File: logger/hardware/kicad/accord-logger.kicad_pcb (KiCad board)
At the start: 2 copper layers, 120 x 80 mm, 87 parts, among them J1 Board connector 14-way, J3 Spare GP13 / switched power, J4 Reset RUN-GND, J5 SD breakout 6-way, Q5 IPD50P04P4L-11, Q6 2N3904, Q7 2N3904, U1 RaspberryPi_Pico_W, U15 MAX3485, U16 DS3231SN, U2 PC817, U3 ASSR-601JV, U6 LM2678T-5.0

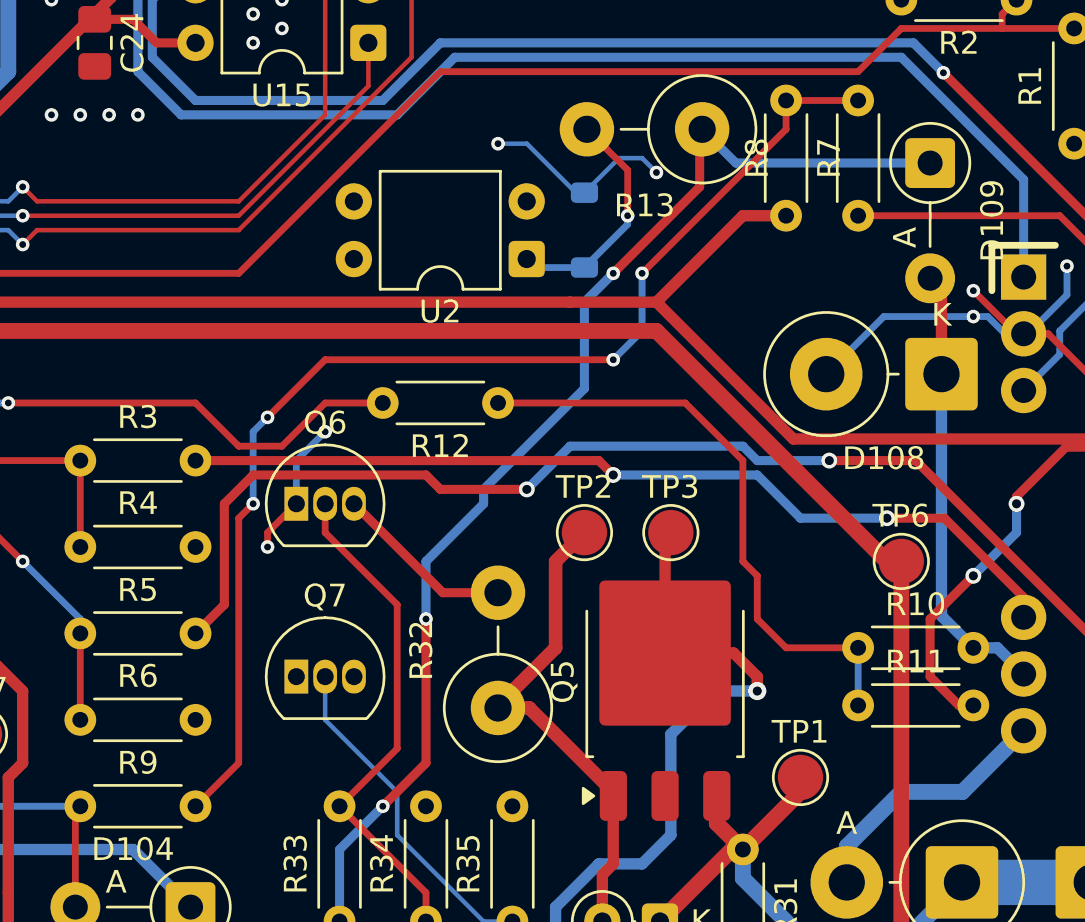
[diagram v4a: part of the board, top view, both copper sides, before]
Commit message: layout: a5_clamp and a5_reg placed and routed
Owner switched on a5_clamp (R22, D111, TP8) and a5_reg (U4, C4, C5, C6,
TP9); eight on_board flags. R22 and D111 sit right of Q5 on P12, TP8 on
the back beside them. U4 TPS70950 on the back by U2, EN open as designed;
C4 at its input (3.1 mm), C5/C6 on A5 between U4 and U2 pin 4. P_AON
runs 0.4 mm from the clamp to U4.

After review: C4 moved from the clamp to U4's input, C5/C6 spaced to
clear their courtyards, FUEL_DIV cleared of the A5 via.

Refilled scratch DRC: parity 0, no errors beyond the Pico footprint's own
paste items, unconnected only Q5's middle lead. ERC 0; full-netlist
capture 782/782; closure 67/67.

Claude-Session-ID: d2c32eb9-406b-48d8-b5b5-bb1d8d4746af
Co-Authored-By: Claude Opus 5.5 <noreply@anthropic.com>
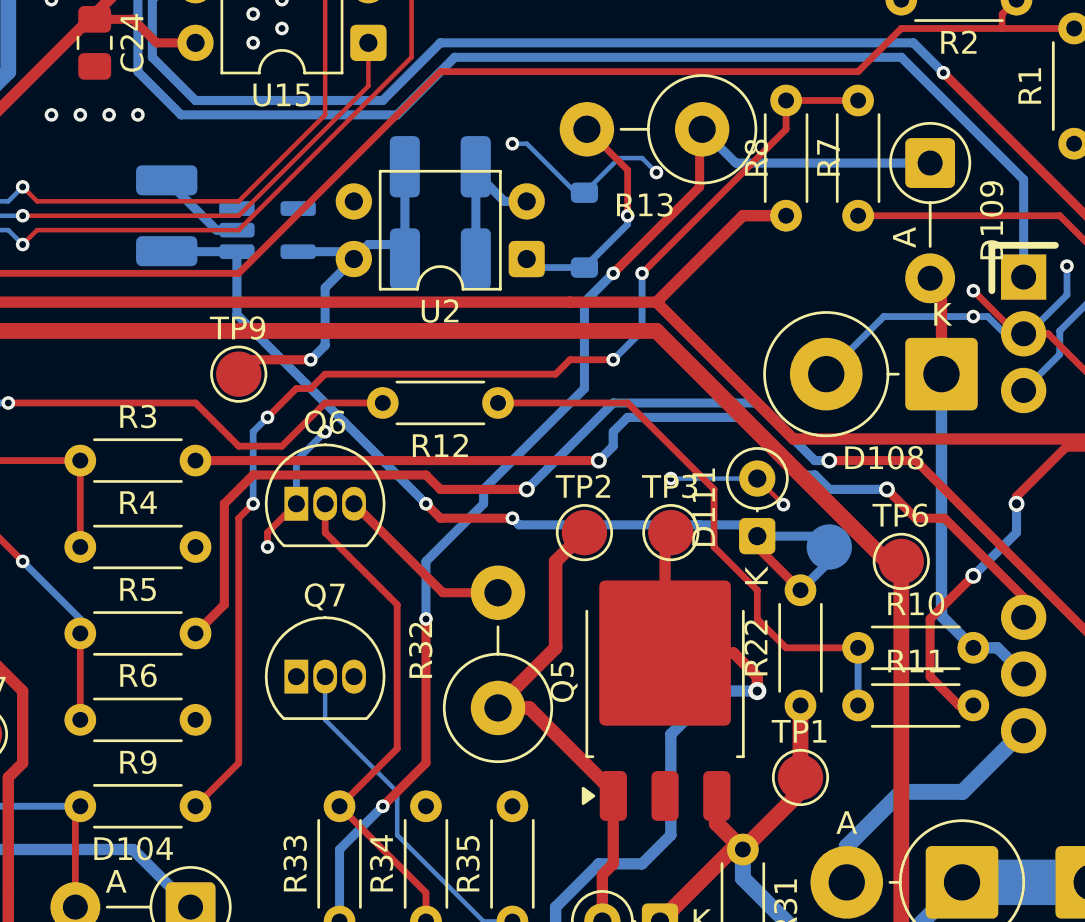
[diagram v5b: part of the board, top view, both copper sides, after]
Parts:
- added C4: 4.7uF/50V, Capacitor_SMD:C_1210_3225Metric_Pad1.33x2.70mm_HandSolder, B.Cu at (148.0, 87.0)
- added C5: 4.7uF/50V, Capacitor_SMD:C_1210_3225Metric_Pad1.33x2.70mm_HandSolder, B.Cu at (160.0, 84.8)
- added C6: 4.7uF/50V, Capacitor_SMD:C_1210_3225Metric_Pad1.33x2.70mm_HandSolder, B.Cu at (160.0, 88.9)
- added D111: BZX55C22, Diode_THT:D_DO-35_SOD27_P2.54mm_Vertical_KathodeUp, F.Cu at (174.0, 101.1)
- added R22: 820R, Resistor_THT:R_Axial_DIN0204_L3.6mm_D1.6mm_P5.08mm_Horizontal, F.Cu at (175.9, 108.6)
- added TP8: TestPoint, TestPoint:TestPoint_Pad_D2.0mm, B.Cu at (177.2, 101.6)
- added TP9: TestPoint, TestPoint:TestPoint_Pad_D2.0mm, F.Cu at (151.1, 94.0)
- added U4: TPS70950QDBVRQ1, Package_TO_SOT_SMD:SOT-23-5_HandSoldering, B.Cu at (152.4, 87.6)
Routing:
- net /P_AON: track 0.00 -> 41.8 mm, vias 0 -> 2
- net /A5: track 0.00 -> 16.9 mm, vias 0 -> 1
- net /PGND: track 79.9 -> 94.6 mm, vias 27 -> 29
- net /P12: track 34.5 -> 37.7 mm
- net /B1_TAP: track 39.9 -> 41.8 mm
- net /C14_TAP: track 53.2 -> 54.8 mm
- net /SUPPLY_DIV: track 26.6 -> 25.1 mm

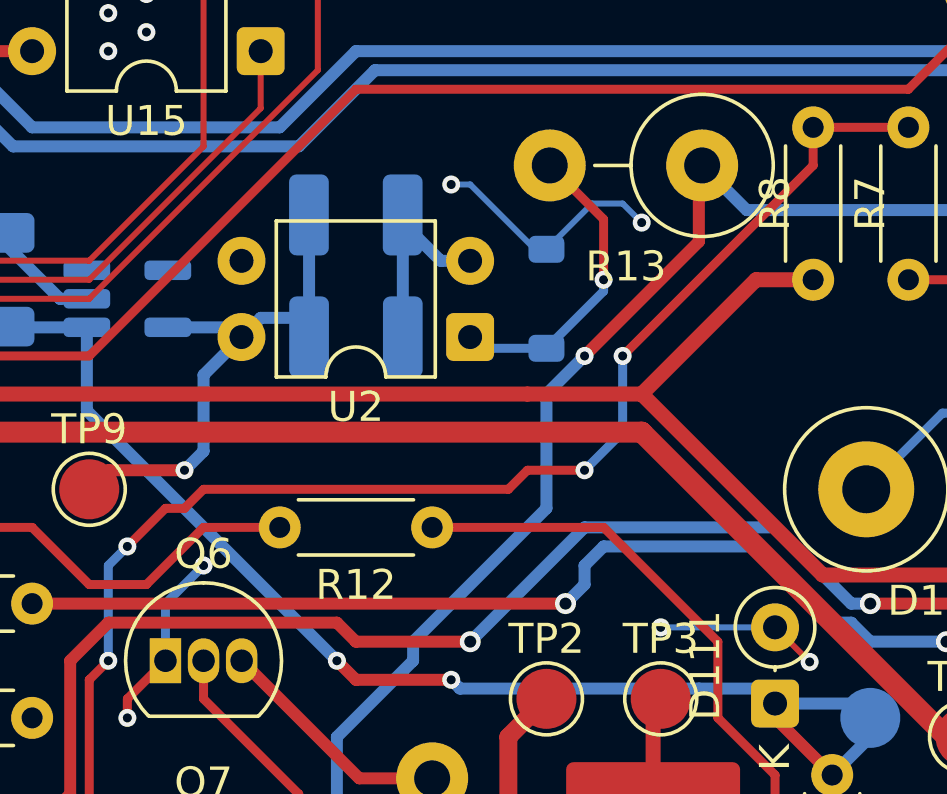
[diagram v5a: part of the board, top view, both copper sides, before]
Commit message: layout: a5_supervisor placed and routed
Owner switched on a5_supervisor (U5, C7, TP17; three on_board flags).
U5 TPS3839 on the back below C6, 8 mm from U4's output; PGOOD runs from
U5 pin 2 to TP17, toward U3 where Q3 goes next.

After review: C7 moved from beside C5 to U5 (pin 1 1.8 mm from U5 pin 3;
ground through the pour).

Refilled scratch DRC: parity 0, no errors beyond the Pico footprint's own
paste items, unconnected only Q5's middle lead. ERC 0; full-netlist
capture 782/782; closure 67/67.

Claude-Session-ID: d2c32eb9-406b-48d8-b5b5-bb1d8d4746af
Co-Authored-By: Claude Opus 5.5 <noreply@anthropic.com>
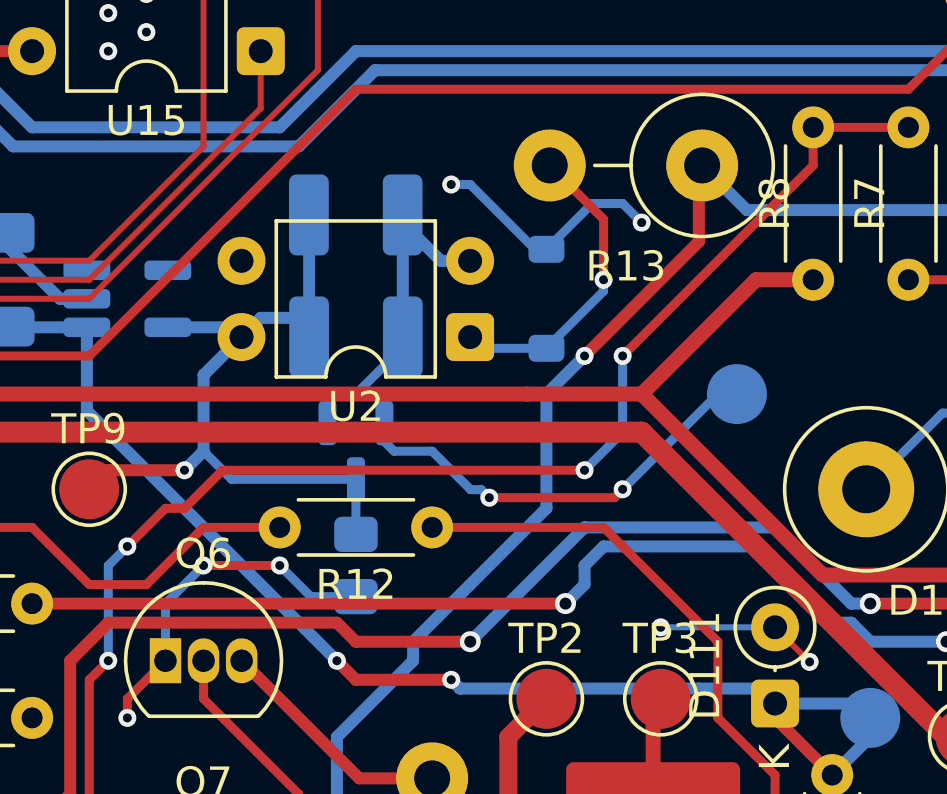
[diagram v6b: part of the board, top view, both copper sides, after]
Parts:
- added C7: 100nF, Capacitor_SMD:C_0805_2012Metric_Pad1.18x1.45mm_HandSolder, B.Cu at (160.0, 96.5)
- added TP17: TestPoint, TestPoint:TestPoint_Pad_D2.0mm, B.Cu at (172.7, 90.8)
- added U5: TPS3839K50DBZR, Package_TO_SOT_SMD:SOT-23, B.Cu at (160.0, 92.7)
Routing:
- net /PGOOD: track 0.00 -> 14.6 mm, vias 0 -> 2
- net /PGND: track 94.6 -> 104.4 mm, vias 29 -> 30
- net /A5: track 16.9 -> 24.7 mm

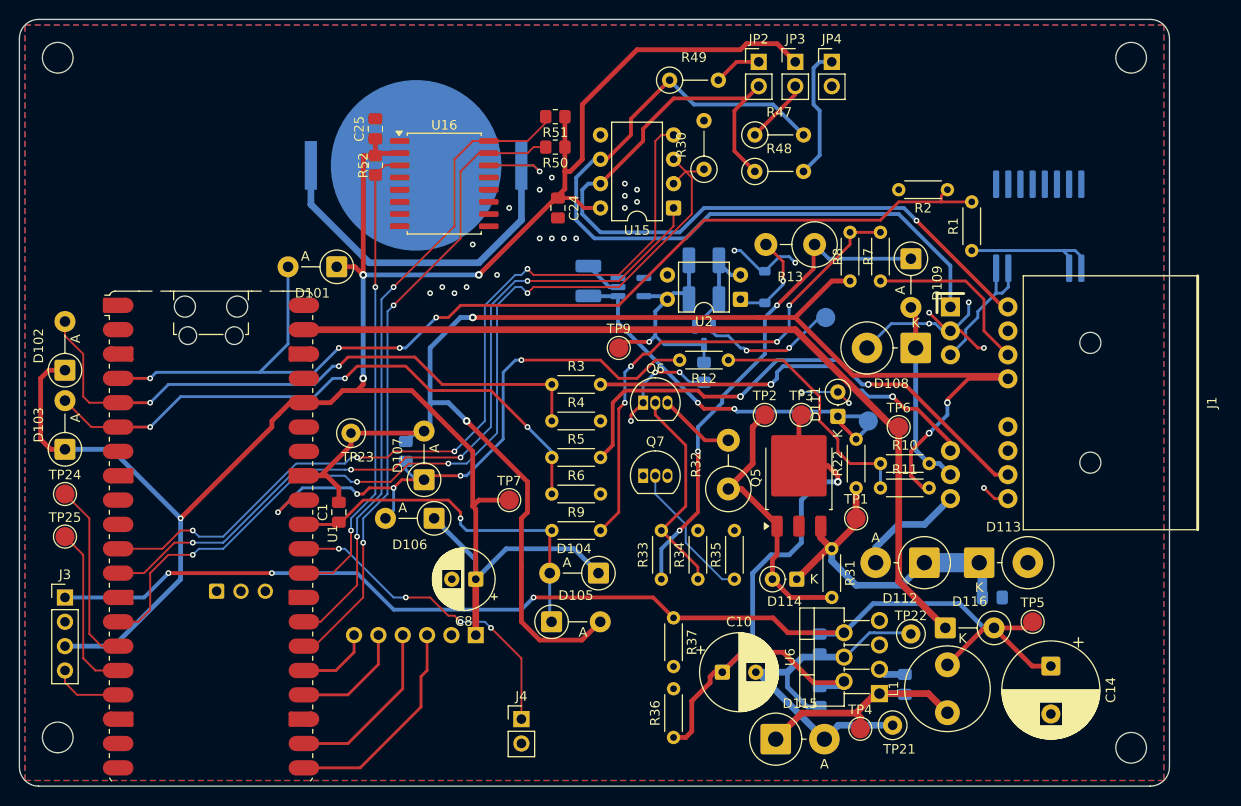
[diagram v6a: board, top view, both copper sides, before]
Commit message: layout: iso_enable and the ignition qualifier placed and routed
Owner switched on iso_enable, qual_rc, qual_reset and qual_report (21
on_board flags). Q3/Q4 with their gate resistors above U3; GP7 (ISO_EN)
routed 113 mm from Pico pin 10 to R24; R23 by the B5 source at the
bottom right. R14, R15, C3, TP12 and Q1 with R16-R18 in the upper
right, where the Schmitt gates will go. Q2 on the back under the Pico
with R21 and TP11 at GP5; R19/R20 at the top left.

After review: ISO_EN and ISO_EN_G completed, RST_B routed, U1 pin 38
thermal relief restored. The owner removed TP24/TP25 from the board;
they move to J3 as a 2x03 (DECISIONS D-HDR-16, recorded here), so DRC
parity lists only those two until the schematic change lands. The
.kicad_pro change is KiCad's default pad size from the owner's session.

Refilled scratch DRC: no errors beyond the Pico footprint's own paste
items, unconnected only Q5's middle lead. ERC 0; full-netlist capture
782/782; closure 67/67.

Claude-Session-ID: d2c32eb9-406b-48d8-b5b5-bb1d8d4746af
Co-Authored-By: Claude Opus 5.5 <noreply@anthropic.com>
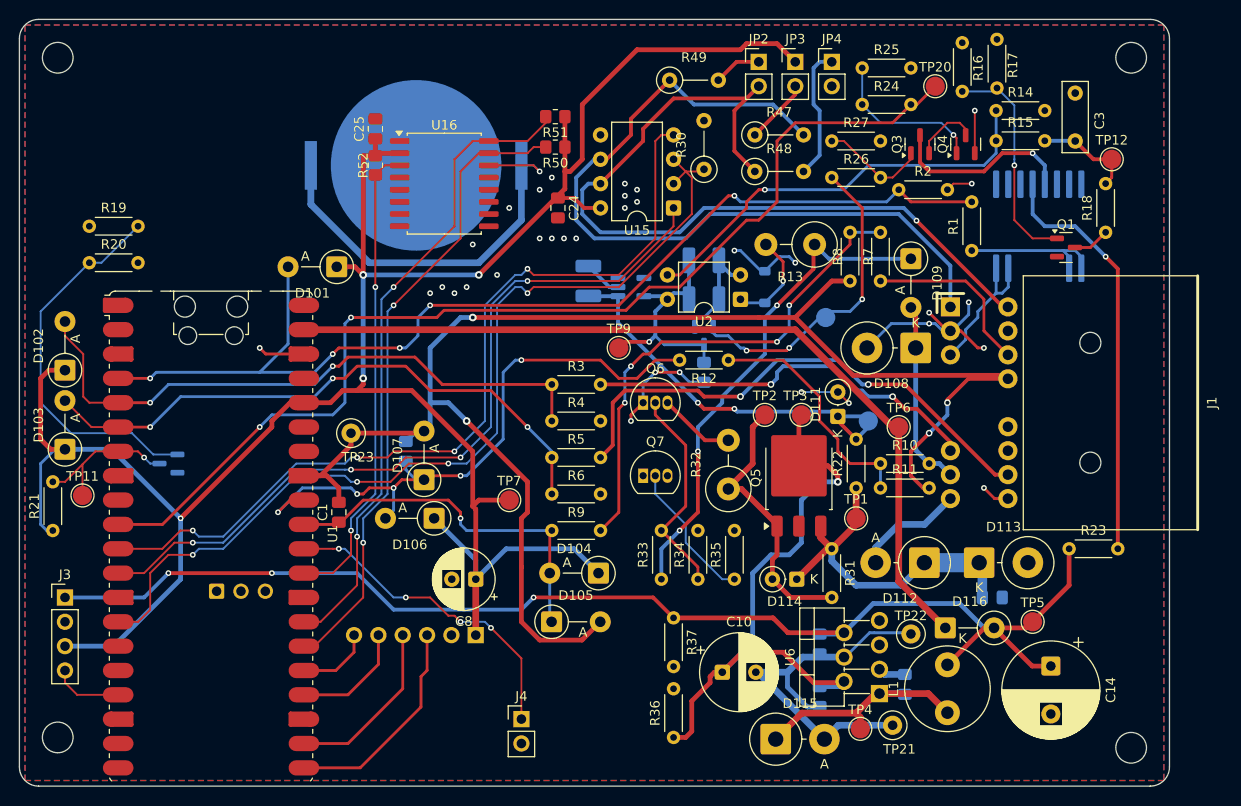
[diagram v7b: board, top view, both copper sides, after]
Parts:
- removed TP24, TP25: TestPoint, TestPoint:TestPoint_Pad_D2.0mm
- added C3: 1uF, Capacitor_THT:C_Rect_L7.2mm_W2.5mm_P5.00mm_FKS2_FKP2_MKS2_MKP2, F.Cu at (198.8, 72.4)
- added Q1: MMBT3904, Package_TO_SOT_SMD:SOT-23, F.Cu at (197.8, 83.5)
- added Q2: BSS138P, Package_TO_SOT_SMD:SOT-23, B.Cu at (104.1, 106.0)
- added Q3: BSS138P, Package_TO_SOT_SMD:SOT-23, F.Cu at (182.6, 72.7)
- added Q4: BSS138P, Package_TO_SOT_SMD:SOT-23, F.Cu at (187.3, 72.7)
- added R14: 47k, Resistor_THT:R_Axial_DIN0204_L3.6mm_D1.6mm_P5.08mm_Horizontal, F.Cu at (190.5, 69.2)
- added R15: 220k, Resistor_THT:R_Axial_DIN0204_L3.6mm_D1.6mm_P5.08mm_Horizontal, F.Cu at (190.5, 72.4)
- added R16: 22k, Resistor_THT:R_Axial_DIN0204_L3.6mm_D1.6mm_P5.08mm_Horizontal, F.Cu at (187.0, 62.1)
- added R17: 100k, Resistor_THT:R_Axial_DIN0204_L3.6mm_D1.6mm_P5.08mm_Horizontal, F.Cu at (190.6, 66.9)
- added R18: 4.7k, Resistor_THT:R_Axial_DIN0204_L3.6mm_D1.6mm_P5.08mm_Horizontal, F.Cu at (201.9, 81.9)
- added R19: 1k, Resistor_THT:R_Axial_DIN0204_L3.6mm_D1.6mm_P5.08mm_Horizontal, F.Cu at (95.9, 81.3)
- added R20: 100k, Resistor_THT:R_Axial_DIN0204_L3.6mm_D1.6mm_P5.08mm_Horizontal, F.Cu at (95.9, 85.1)
- added R21: 10k, Resistor_THT:R_Axial_DIN0204_L3.6mm_D1.6mm_P5.08mm_Horizontal, F.Cu at (92.1, 113.0)
- added R23: 270R, Resistor_THT:R_Axial_DIN0204_L3.6mm_D1.6mm_P5.08mm_Horizontal, F.Cu at (198.1, 114.9)
- added R24: 1k, Resistor_THT:R_Axial_DIN0204_L3.6mm_D1.6mm_P5.08mm_Horizontal, F.Cu at (181.6, 68.6)
- added R25: 100k, Resistor_THT:R_Axial_DIN0204_L3.6mm_D1.6mm_P5.08mm_Horizontal, F.Cu at (176.5, 64.8)
- added R26: 1k, Resistor_THT:R_Axial_DIN0204_L3.6mm_D1.6mm_P5.08mm_Horizontal, F.Cu at (173.4, 76.2)
- added R27: 100k, Resistor_THT:R_Axial_DIN0204_L3.6mm_D1.6mm_P5.08mm_Horizontal, F.Cu at (173.4, 72.4)
- added TP11: TestPoint, TestPoint:TestPoint_Pad_D2.0mm, F.Cu at (95.2, 109.4)
- added TP12: TestPoint, TestPoint:TestPoint_Pad_D2.0mm, F.Cu at (202.6, 74.3)
- added TP20: TestPoint, TestPoint:TestPoint_Pad_D2.0mm, F.Cu at (184.2, 66.7)
- moved R2 5.08 mm to (180.3, 77.5), turned to 0 degrees
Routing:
- net /ISO_EN: track 0.00 -> 112.8 mm, vias 0 -> 2
- net /IGN_A: track 0.00 -> 44.4 mm, vias 0 -> 1
- net /ISO_LED_A: track 0.00 -> 43.6 mm, vias 0 -> 1
- net /REP_G: track 0.00 -> 39.9 mm
- net /RST_B: track 0.00 -> 23.5 mm, vias 0 -> 1
- net /ISO_LED_K: track 0.00 -> 19.5 mm, vias 0 -> 1
- net /SPARE_GP11: track 19.2 -> 0.00 mm
- net /PGOOD: track 14.6 -> 33.2 mm, vias 2 -> 3
- net /SPARE_GP12: track 17.7 -> 0.00 mm
- net /ISO_EN_G: track 0.00 -> 16.7 mm, vias 0 -> 1
- net /QUAL_N_REPORT: track 0.00 -> 16.2 mm, vias 0 -> 1
- net /PGND: track 104.4 -> 116.6 mm, vias 30 -> 33
- net /ISO_PG_G: track 0.00 -> 11.3 mm
- net /P3V3_SW: track 239.0 -> 250.1 mm
- net /IGN_RC: track 0.00 -> 10.6 mm
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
